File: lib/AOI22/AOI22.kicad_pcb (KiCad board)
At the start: 2 copper layers, 8 parts, among them P1 Q_PJFET_GSD, P2 Q_PJFET_GSD, P3 Q_PJFET_GSD, P4 Q_PJFET_GSD

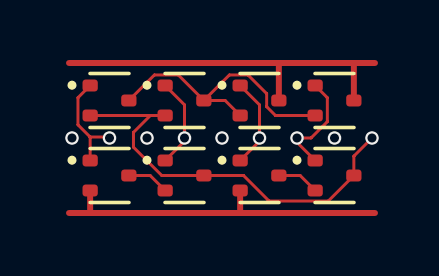
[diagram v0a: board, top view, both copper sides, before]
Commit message: Move pin definition to gate's physical .v
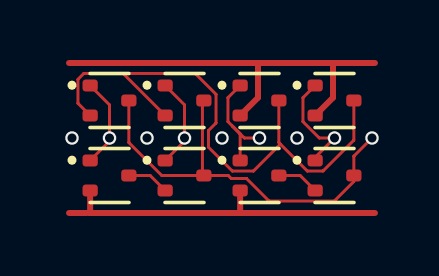
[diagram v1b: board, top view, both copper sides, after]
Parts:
- N1, N2, N3, N4: value Q_NJFET_GSD -> (none)
- P1, P2, P3, P4: value Q_PJFET_GSD -> (none)
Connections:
- net A renamed A1
- net B renamed A2
- net C renamed B1
- net D renamed B2
- net Net-(N1-D) renamed intA
- net Net-(N3-D) renamed intB
- P1 pad 2: Y -> intP
- P1 pad 3: Net-(P1-D) -> Y
- P2 pad 2: Y -> intP
- P2 pad 3: Net-(P1-D) -> Y
- P3 pad 2: Net-(P1-D) -> VDD
- P3 pad 3: VDD -> intP
- P4 pad 2: Net-(P1-D) -> VDD
- P4 pad 3: VDD -> intP
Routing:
- net intP: track 0.00 -> 19.4 mm
- net Net-(P1-D): track 9.50 -> 0.00 mm
- net VDD: track 12.7 -> 14.2 mm
- net B1: track 3.03 -> 4.01 mm

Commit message: High-density layout with pitch of 1.1mm, which gains 23% !!
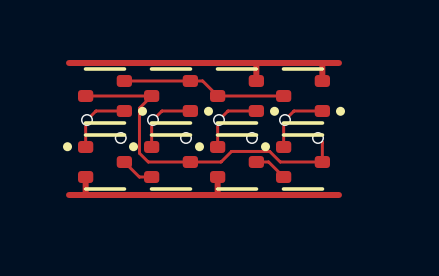
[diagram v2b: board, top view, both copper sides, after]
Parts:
- moved N4 1.14 mm to (7.70, 3.30)
- moved P4 1.06 mm to (7.70, 1.10), turned to 180 degrees
- moved N3 0.87 mm to (5.50, 3.30)
- moved P3 0.76 mm to (5.50, 1.10), turned to 180 degrees
- moved N2 0.64 mm to (3.30, 3.30)
- moved N1 0.47 mm to (1.10, 3.30)
- moved P2 0.47 mm to (3.30, 1.10), turned to 180 degrees
- moved P1 0.21 mm to (1.10, 1.10), turned to 180 degrees
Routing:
- net intP: track 19.4 -> 5.52 mm
- net VDD: track 14.2 -> 10.2 mm
- net Y: track 14.2 -> 11.6 mm
- net B1: track 4.01 -> 2.29 mm
- net B2: track 3.67 -> 2.29 mm
- net GND: track 11.6 -> 10.2 mm
- net A2: track 3.03 -> 2.29 mm
- net A1: track 3.03 -> 2.29 mm
- net (no net): vias 4 -> 3

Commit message: All cells now use 1mm*4mm grid rather than 1.1mm*4.4mm
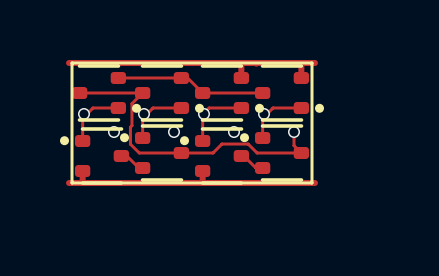
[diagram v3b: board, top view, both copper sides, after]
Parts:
- moved N4 0.76 mm to (7.00, 3.00)
- moved P4 0.71 mm to (7.00, 1.00)
- moved N3 0.54 mm to (5.00, 3.10)
- moved P3 0.51 mm to (5.00, 1.00)
- moved N2 0.42 mm to (3.00, 3.00)
- moved P2 0.32 mm to (3.00, 1.00)
- moved P1 0.22 mm to (0.90, 1.00)
- moved N1 0.22 mm to (1.00, 3.10)
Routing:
- net GND: track 10.2 -> 9.24 mm
- net Y: track 11.6 -> 10.7 mm
- net VDD: track 10.2 -> 9.28 mm

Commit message: Use my own SOT-523 footprint, removing distracting silkscreen markings. Apply it to AOI22
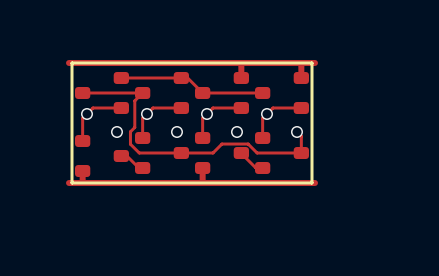
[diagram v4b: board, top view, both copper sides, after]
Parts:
- N1, N2, N3, N4, P1, P2, P3, P4: footprint Package_TO_SOT_SMD:SOT-523 -> RV523:SOT523
- moved N3 0.10 mm to (5.00, 3.00)
- moved P1 0.10 mm to (1.00, 1.00)

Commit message: Experiment with pads at Y=1.8/2.2 rather than 1.7/2.3 and not moving the transistors up and down, otherwise, Y-clearance of 0.4mm cannot be ensured
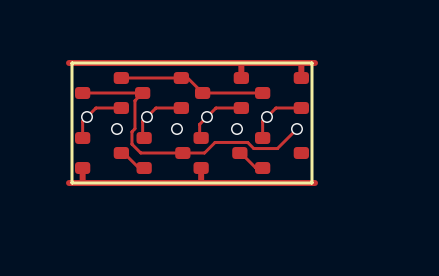
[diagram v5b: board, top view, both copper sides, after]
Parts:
- moved N1 0.10 mm to (1.00, 3.00)
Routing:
- net Y: track 10.6 -> 10.0 mm
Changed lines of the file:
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@@
 	(footprint "RV523:SOT523"
 		(layer "F.Cu")
-		(at 3 3)
+		(at 3.05 3)
 		(descr "SOT523, https://www.diodes.com/assets/Package-Files/SOT523.pdf")
 		(tags "SOT-523")
@@
 	(footprint "RV523:SOT523"
 		(layer "F.Cu")
-		(at 1 3.1)
+		(at 1 3)
 		(descr "SOT523, https://www.diodes.com/assets/Package-Files/SOT523.pdf")
 		(tags "SOT-523")
@@
 	(footprint "RV523:SOT523"
 		(layer "F.Cu")
-		(at 5 3)
+		(at 4.95 3)
 		(descr "SOT523, https://www.diodes.com/assets/Package-Files/SOT523.pdf")
 		(tags "SOT-523")
@@
 	)
 	(via
-		(at 1.5 2.3)
+		(at 1.5 2.2)
 		(size 0.4)
 		(drill 0.3)
@@
 	)
 	(via
-		(at 3.5 2.3)
+		(at 3.5 2.2)
 		(size 0.4)
 		(drill 0.3)
@@
 	)
 	(via
-		(at 5.5 2.3)
+		(at 5.5 2.2)
 		(size 0.4)
 		(drill 0.3)
@@
 	)
 	(segment
+		(start 4.305 3.5)
+		(end 4.305 3.975)
+		(width 0.2)
+		(layer "F.Cu")
+		(net 2)
+	)
+	(segment
 		(start 0.355 3.955)
 		(end 0.4 4)
@@
 	)
 	(segment
-		(start 4.355 3.5)
-		(end 4.355 3.955)
-		(width 0.2)
-		(layer "F.Cu")
-		(net 2)
-	)
-	(segment
-		(start 4.355 3.955)
-		(end 4.4 4)
-		(width 0.2)
-		(layer "F.Cu")
-		(net 2)
-	)
-	(segment
 		(start 0.355 3.5)
 		(end 0.355 3.955)
@@
 	)
 	(segment
+		(start 4.305 3.975)
+		(end 4.28 4)
+		(width 0.2)
+		(layer "F.Cu")
+		(net 2)
+	)
+	(segment
+		(start 4.28 4)
+		(end 4.4 4)
+		(width 0.2)
+		(layer "F.Cu")
+		(net 2)
+	)
+	(segment
 		(start 0.4 4)
-		(end 4.4 4)
+		(end 4.28 4)
 		(width 0.2)
 		(layer "F.Cu")
@@
 	)
 	(segment
+		(start 0.355 1.945)
+		(end 0.5 1.8)
+		(width 0.1)
+		(layer "F.Cu")
+		(net 3)
+	)
+	(segment
+		(start 0.8 1.5)
+		(end 0.5 1.8)
+		(width 0.1)
+		(layer "F.Cu")
+		(net 3)
+	)
+	(segment
 		(start 1.645 1.5)
-		(end 0.7 1.5)
+		(end 0.8 1.5)
 		(width 0.1)
 		(layer "F.Cu")
@@
 	)
 	(segment
-		(start 0.355 1.845)
-		(end 0.5 1.7)
+		(start 0.355 2.5)
+		(end 0.355 1.945)
 		(width 0.1)
 		(layer "F.Cu")
 		(net 3)
 	)
-	(segment
-		(start 0.7 1.5)
-		(end 0.5 1.7)
-		(width 0.1)
-		(layer "F.Cu")
-		(net 3)
-	)
-	(segment
-		(start 0.355 2.6)
-		(end 0.355 1.845)
-		(width 0.1)
-		(layer "F.Cu")
-		(net 3)
-	)
 	(via
-		(at 0.5 1.7)
+		(at 0.5 1.8)
 		(size 0.4)
 		(drill 0.3)
@@
 	)
 	(segment
+		(start 2.8 1.5)
+		(end 2.5 1.8)
+		(width 0.1)
+		(layer "F.Cu")
+		(net 4)
+	)
+	(segment
 		(start 3.645 1.5)
-		(end 2.7 1.5)
+		(end 2.8 1.5)
 		(width 0.1)
 		(layer "F.Cu")
@@
 	(segment
 		(start 2.355 2.5)
-		(end 2.355 1.845)
+		(end 2.355 1.945)
 		(width 0.1)
 		(layer "F.Cu")
@@
 	)
 	(segment
-		(start 2.7 1.5)
-		(end 2.5 1.7)
+		(start 2.355 1.945)
+		(end 2.5 1.8)
 		(width 0.1)
 		(layer "F.Cu")
 		(net 4)
 	)
-	(segment
-		(start 2.355 1.845)
-		(end 2.5 1.7)
-		(width 0.1)
-		(layer "F.Cu")
-		(net 4)
-	)
 	(via
-		(at 2.5 1.7)
+		(at 2.5 1.8)
 		(size 0.4)
 		(drill 0.3)
@@
 	)
 	(segment
-		(start 2.093262 1.261738)
-		(end 2.093262 2.149)
+		(start 6.058738 2.851)
+		(end 5.856738 2.649)
 		(width 0.1)
 		(layer "F.Cu")
@@
 	)
 	(segment
-		(start 1.949 2.706738)
-		(end 2.242262 3)
+		(start 1.999 2.293262)
+		(end 1.999 2.706738)
 		(width 0.1)
 		(layer "F.Cu")
@@
 	)
 	(segment
-		(start 4.7 3)
-		(end 3.705 3)
+		(start 1.999 2.706738)
+		(end 2.292262 3)
 		(width 0.1)
 		(layer "F.Cu")
@@
 	)
 	(segment
-		(start 6.17 3)
-		(end 5.871 2.701)
+		(start 5.856738 2.649)
+		(end 4.768738 2.649)
 		(width 0.1)
 		(layer "F.Cu")
@@
 	)
 	(segment
-		(start 1.949 2.293262)
-		(end 1.949 2.706738)
+		(start 2.355 1)
+		(end 2.099 1.256)
 		(width 0.1)
 		(layer "F.Cu")
@@
 	)
 	(segment
-		(start 7.645 3)
-		(end 6.17 3)
+		(start 2.099 2.193262)
+		(end 1.999 2.293262)
 		(width 0.1)
 		(layer "F.Cu")
@@
 	)
 	(segment
-		(start 4.999 2.701)
-		(end 4.7 3)
-		(width 0.1)
-		(layer "F.Cu")
-		(net 5)
-	)
-	(segment
-		(start 2.355 1)
-		(end 2.093262 1.261738)
-		(width 0.1)
-		(layer "F.Cu")
-		(net 5)
-	)
-	(segment
-		(start 7.645 2.445)
-		(end 7.5 2.3)
-		(width 0.1)
-		(layer "F.Cu")
-		(net 5)
-	)
-	(segment
-		(start 7.645 3)
-		(end 7.645 2.445)
-		(width 0.1)
-		(layer "F.Cu")
-		(net 5)
-	)
-	(segment
-		(start 2.242262 3)
-		(end 3.645 3)
+		(start 2.292262 3)
+		(end 3.695 3)
 		(width 0.1)
 		(layer "F.Cu")
@@
 	)
 	(segment
-		(start 2.093262 2.149)
-		(end 1.949 2.293262)
+		(start 4.768738 2.649)
+		(end 4.417738 3)
 		(width 0.1)
 		(layer "F.Cu")
@@
 	)
 	(segment
-		(start 5.871 2.701)
-		(end 4.999 2.701)
+		(start 2.099 1.256)
+		(end 2.099 2.193262)
 		(width 0.1)
 		(layer "F.Cu")
 		(net 5)
 	)
+	(segment
+		(start 6.849 2.851)
+		(end 6.058738 2.851)
+		(width 0.1)
+		(layer "F.Cu")
+		(net 5)
+	)
+	(segment
+		(start 4.417738 3)
+		(end 3.645 3)
+		(width 0.1)
+		(layer "F.Cu")
+		(net 5)
+	)
+	(segment
+		(start 7.5 2.2)
+		(end 6.849 2.851)
+		(width 0.1)
+		(layer "F.Cu")
+		(net 5)
+	)
 	(via
-		(at 7.5 2.3)
+		(at 7.5 2.2)
 		(size 0.4)
 		(drill 0.3)
@@
 	)
 	(segment
-		(start 4.355 1.845)
-		(end 4.5 1.7)
+		(start 4.8 1.5)
+		(end 4.5 1.8)
 		(width 0.1)
 		(layer "F.Cu")
@@
 	)
 	(segment
+		(start 4.255 2.5)
+		(end 4.255 2.045)
+		(width 0.1)
+		(layer "F.Cu")
+		(net 6)
+	)
+	(segment
+		(start 4.255 2.045)
+		(end 4.5 1.8)
+		(width 0.1)
+		(layer "F.Cu")
+		(net 6)
+	)
+	(segment
 		(start 5.645 1.5)
-		(end 4.7 1.5)
+		(end 4.8 1.5)
 		(width 0.1)
 		(layer "F.Cu")
 		(net 6)
 	)
-	(segment
-		(start 4.7 1.5)
-		(end 4.5 1.7)
-		(width 0.1)
-		(layer "F.Cu")
-		(net 6)
-	)
-	(segment
-		(start 4.355 2.6)
-		(end 4.355 1.845)
-		(width 0.1)
-		(layer "F.Cu")
-		(net 6)
-	)
 	(via
-		(at 4.5 1.7)
+		(at 4.5 1.8)
 		(size 0.4)
 		(drill 0.3)
@@
 	(segment
 		(start 6.355 2.5)
-		(end 6.355 1.845)
+		(end 6.355 1.945)
 		(width 0.1)
 		(layer "F.Cu")
@@
 	)
 	(segment
-		(start 6.7 1.5)
-		(end 6.5 1.7)
+		(start 7.645 1.5)
+		(end 6.8 1.5)
 		(width 0.1)
 		(layer "F.Cu")
@@
 	)
 	(segment
-		(start 6.355 1.845)
-		(end 6.5 1.7)
+		(start 6.8 1.5)
+		(end 6.5 1.8)
 		(width 0.1)
 		(layer "F.Cu")
@@
 	)
 	(segment
-		(start 7.645 1.5)
-		(end 6.7 1.5)
+		(start 6.355 1.945)
+		(end 6.5 1.8)
 		(width 0.1)
 		(layer "F.Cu")
@@
 	)
 	(via
-		(at 6.5 1.7)
+		(at 6.5 1.8)
 		(size 0.4)
 		(drill 0.3)

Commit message: Make the pads of my SOT523 footprint very slightly smaller, which is enough to route all the cells and leave the mosfets exactly on the grid
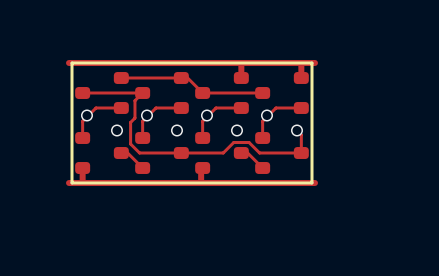
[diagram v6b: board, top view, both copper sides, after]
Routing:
- net Y: track 10.0 -> 10.8 mm

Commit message: Propagate MOSFET values to the cells' PCBs
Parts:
- N1, N2, N3, N4: value (none) -> NMOS
- P1, P2, P3, P4: value (none) -> PMOS
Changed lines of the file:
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@@
 			)
 		)
-		(property "Value" ""
+		(property "Value" "PMOS"
 			(at 0 0 180)
 			(layer "F.Fab")
@@
 			)
 		)
-		(property "Value" ""
+		(property "Value" "NMOS"
 			(at 0 0 0)
 			(layer "F.Fab")
@@
 			)
 		)
-		(property "Value" ""
+		(property "Value" "NMOS"
 			(at 0 0 0)
 			(layer "F.Fab")
@@
 			)
 		)
-		(property "Value" ""
+		(property "Value" "PMOS"
 			(at 0 0 180)
 			(layer "F.Fab")
@@
 			)
 		)
-		(property "Value" ""
+		(property "Value" "PMOS"
 			(at 0 0 180)
 			(layer "F.Fab")
@@
 			)
 		)
-		(property "Value" ""
+		(property "Value" "PMOS"
 			(at 0 0 180)
 			(layer "F.Fab")
@@
 			)
 		)
-		(property "Value" ""
+		(property "Value" "NMOS"
 			(at 0 0 0)
 			(layer "F.Fab")
@@
 			)
 		)
-		(property "Value" ""
-			(at 0 0 0)
-			(layer "F.Fab")
+		(property "Value" "NMOS"
+			(at 0 0 0)
+			(layer "F.Fab")
